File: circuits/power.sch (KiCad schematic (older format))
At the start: 37 parts, among them J5 Barrel_Jack_OD5.5_ID2.5, J6 Barrel_Jack_OD5.5_ID2.5, J7 Barrel_Jack_OD5.5_ID2.5, U4 REG_3V3, U5 MIC29302WU, U6 MIC29302WU, U7 MIC29302WU

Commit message: Sent to fab.
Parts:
- removed C1: C_1000uF, Capacitor_THT:CP_Radial_D12.5mm_P5.00mm, symbol Open_Automation:C_1000uF
- removed C2, C6: C_10uF, Capacitor_SMD:C_0603_1608Metric_Pad1.08x0.95mm_HandSolder, symbol Open_Automation:C_10uF
- removed C7, C8, C9: C_10uF_Ta, Capacitor_Tantalum_SMD:CP_EIA-6032-15_Kemet-U_Pad2.25x2.35mm_HandSolder, symbol Open_Automation:C_10uF_Ta
- removed D2: D_Zener, Diode_SMD:D_SMB_Handsoldering, symbol Open_Automation:D_Zener
- removed D4, D5, D6, D7: LED_G, LED_SMD:LED_0603_1608Metric_Pad1.05x0.95mm_HandSolder, symbol Open_Automation:LED_G
- removed J5, J6, J7: Barrel_Jack_OD5.5_ID2.5, Open_Automation:BarrelJack_OD5.5_ID2.5, symbol Open_Automation:Barrel_Jack_OD5.5_ID2.5
- removed R10, R11, R20, R7: R_1K, Resistor_SMD:R_0603_1608Metric_Pad0.98x0.95mm_HandSolder, symbol Open_Automation:R_1K
- removed R12, R13, R4: R_10K, Resistor_SMD:R_0603_1608Metric_Pad0.98x0.95mm_HandSolder, symbol Open_Automation:R_10K
- removed R14, R16, R18: R_20K, Resistor_SMD:R_0603_1608Metric_Pad0.98x0.95mm_HandSolder, symbol Open_Automation:R_20K
- removed R15: R_6.5K, Resistor_SMD:R_0603_1608Metric_Pad0.98x0.95mm_HandSolder, symbol Open_Automation:R_6.5K
- removed R17: R_2.2K, Resistor_SMD:R_0603_1608Metric_Pad0.98x0.95mm_HandSolder, symbol Open_Automation:R_2.2K
- removed R3: R_100K, Resistor_SMD:R_0603_1608Metric_Pad0.98x0.95mm_HandSolder, symbol Open_Automation:R_100K
- removed U6, U7: MIC29302WU, Package_TO_SOT_SMD:TO-263-5_TabPin3, symbol Open_Automation:MIC29302WU
- added C1: C_10uF, Capacitor_SMD:C_0603_1608Metric_Pad1.08x0.95mm_HandSolder, symbol Open_Automation:C_10uF
- added C2, C6: C_10uF_Ta, Capacitor_Tantalum_SMD:CP_EIA-6032-15_Kemet-U_Pad2.25x2.35mm_HandSolder, symbol Open_Automation:C_10uF_Ta
- added D1: D_Zener, Diode_SMD:D_SMB_Handsoldering, symbol Open_Automation:D_Zener
- added D2: LED_G, LED_SMD:LED_0603_1608Metric_Pad1.05x0.95mm_HandSolder, symbol Open_Automation:LED_G
- added J10: Barrel_Jack_OD5.5_ID2.5, Open_Automation:BarrelJack_OD5.5_ID2.5, symbol Open_Automation:Barrel_Jack_OD5.5_ID2.5
- added R31, R37: R_20K, Resistor_SMD:R_0603_1608Metric_Pad0.98x0.95mm_HandSolder, symbol Open_Automation:R_20K
- added R32: R_6.5K, Resistor_SMD:R_0603_1608Metric_Pad0.98x0.95mm_HandSolder, symbol Open_Automation:R_6.5K
- added R33, R36: R_1K, Resistor_SMD:R_0603_1608Metric_Pad0.98x0.95mm_HandSolder, symbol Open_Automation:R_1K
- added R34: R_70K, Resistor_SMD:R_0603_1608Metric_Pad0.98x0.95mm_HandSolder, symbol Open_Automation:R_70K
- added R35: R_10K, Resistor_SMD:R_0603_1608Metric_Pad0.98x0.95mm_HandSolder, symbol Open_Automation:R_10K
- added U9: MIC29302WU, Package_TO_SOT_SMD:TO-263-5_TabPin3, symbol Open_Automation:MIC29302WU
- renumbered R19 to R38, R8 to R39, U5 to U7, U4 to U8
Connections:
- net labels added: POWER, PWR_SENSE, REG_POWER
- net labels removed: BATTERY, BATT_ADC, CURRENT_SENSE, DISPLAY_EN, DISPLAY_POWER, MAIN_EN, MAIN_POWER, MAIN_POWER_IN, POWER_IN, SENSE0, SENSE1, TRIGGER0, TRIGGER1, VIOUT
- wire segments 122 -> 70
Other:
- moved on the sheet: R38, R39, U7

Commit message: finished schematic corrections, working on layout
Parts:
- removed D1: D_Zener, Diode_SMD:D_SMB_Handsoldering, symbol Open_Automation:D_Zener
- removed J10: Barrel_Jack_OD5.5_ID2.5, Open_Automation:BarrelJack_OD5.5_ID2.5, symbol Open_Automation:Barrel_Jack_OD5.5_ID2.5
- removed R32: R_6.5K, Resistor_SMD:R_0603_1608Metric_Pad0.98x0.95mm_HandSolder, symbol Open_Automation:R_6.5K
- removed U8: REG_3V3, Package_TO_SOT_SMD:TO-252-2, symbol Open_Automation:REG_3V3
- added D3: LED_G, LED_SMD:LED_0603_1608Metric_Pad1.05x0.95mm_HandSolder, symbol Open_Automation:LED_G
- added R33: R_6.8K, Resistor_SMD:R_0603_1608Metric_Pad0.98x0.95mm_HandSolder, symbol Open_Automation:R_6.8K
- added U8: REG_AMS1117-3.3, Package_TO_SOT_SMD:SOT-223-3_TabPin2, symbol Open_Automation:REG_AMS1117-3.3
- renumbered D3 to D4, R31 to R32, R33 to R34, R34 to R35, R35 to R36, R36 to R37, R37 to R38, R38 to R39, R39 to R40
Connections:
- wire segments 70 -> 66
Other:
- moved on the sheet: R37

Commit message: got board back from fab, testing
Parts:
- removed R32, R38: R_20K, Resistor_SMD:R_0603_1608Metric_Pad0.98x0.95mm_HandSolder, symbol Open_Automation:R_20K
- removed R36: R_10K, Resistor_SMD:R_0603_1608Metric_Pad0.98x0.95mm_HandSolder, symbol Open_Automation:R_10K
- removed R39: R_2.2K, Resistor_SMD:R_0603_1608Metric_Pad0.98x0.95mm_HandSolder, symbol Open_Automation:R_2.2K
- added R?: R_2.2K, Resistor_SMD:R_0402_1005Metric_Pad0.72x0.64mm_HandSolder, symbol Open_Automation:R_2.2K
- added R? (x2): R_20K, Resistor_SMD:R_0402_1005Metric_Pad0.72x0.64mm_HandSolder, symbol Open_Automation:R_20K
- added R?: R_10K_0402, Resistor_SMD:R_0402_1005Metric_Pad0.72x0.64mm_HandSolder, symbol Open_Automation:R_10K_0402
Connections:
- net 5V: now also R?.1
- net GND: now also R?.1, R?.2
- net PWR_SENSE: now also R?.2
- net REG_POWER: now also R?.1
- net at U9.5 (Feedback): now also R?.1, R?.2
- net at R33.1, U7.5 (Feedback): now also R?.2
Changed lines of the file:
@@
-$EndComp
-$Comp
-L Open_Automation:R_20K R?
-U 1 1 5FFACB63
-P 8550 4350
-AR Path="/5A7BADB8/5FFACB63" Ref="R?"  Part="1"
-AR Path="/6045445B/5FFACB63" Ref="R38"  Part="1"
-F 0 "R38" H 8600 4300 50  0000 L CNN
-F 1 "R_20K" H 8550 4200 50  0000 L CNN
-F 2 "Resistor_SMD:R_0603_1608Metric_Pad0.98x0.95mm_HandSolder" V 8480 4350 50  0001 C CNN
-F 3 "https://datasheet.lcsc.com/szlcsc/Uniroyal-Elec-0603WAF2002T5E_C4184.pdf" V 8630 4350 50  0001 C CNN
-F 4 "0603WAF2002T5E" V 8730 4450 60  0001 C CNN "Part Number"
-F 5 "C4184" H -1250 -1150 50  0001 C CNN "LCSC"
-	1    8550 4350
-	1    0    0    -1
-$EndComp
-$Comp
-L Open_Automation:R_20K R?
-U 1 1 5FFACB61
-P 4600 4150
-AR Path="/5A7BADB8/5FFACB61" Ref="R?"  Part="1"
-AR Path="/6045445B/5FFACB61" Ref="R32"  Part="1"
-F 0 "R32" V 4600 4050 50  0000 L CNN
-F 1 "R_20K" V 4700 4050 50  0000 L CNN
-F 2 "Resistor_SMD:R_0603_1608Metric_Pad0.98x0.95mm_HandSolder" V 4530 4150 50  0001 C CNN
-F 3 "https://datasheet.lcsc.com/szlcsc/Uniroyal-Elec-0603WAF2002T5E_C4184.pdf" V 4680 4150 50  0001 C CNN
-F 4 "0603WAF2002T5E" V 4780 4250 60  0001 C CNN "Part Number"
-F 5 "C4184" H -5100 2200 50  0001 C CNN "LCSC"
-	1    4600 4150
-	1    0    0    -1
 $EndComp
 $Comp
@@
 	1    0    0    -1
 $EndComp
-$Comp
-L Open_Automation:R_2.2K R?
-U 1 1 5CC27388
-P 8550 4750
-AR Path="/5A7BADB8/5CC27388" Ref="R?"  Part="1"
-AR Path="/6045445B/5CC27388" Ref="R39"  Part="1"
-F 0 "R39" H 8600 4700 50  0000 L CNN
-F 1 "R_2.2K" H 8550 4600 50  0000 L CNN
-F 2 "Resistor_SMD:R_0603_1608Metric_Pad0.98x0.95mm_HandSolder" V 8480 4750 50  0001 C CNN
-F 3 "https://datasheet.lcsc.com/szlcsc/Uniroyal-Elec-0603WAF2201T5E_C4190.pdf" V 8630 4750 50  0001 C CNN
-F 4 "0603WAF2201T5E" V 8730 4850 60  0001 C CNN "Part Number"
-F 5 "C4190" H -1250 -1150 50  0001 C CNN "LCSC"
-	1    8550 4750
-	1    0    0    -1
-$EndComp
 Wire Wire Line
 	6950 4150 6900 4150
@@
 Text HLabel 1650 1300 0    60   Input ~ 0
 REG_POWER
-$Comp
-L Open_Automation:R_10K R36
-U 1 1 60405BCA
-P 5350 1950
-F 0 "R36" H 5420 1996 50  0000 L CNN
-F 1 "R_10K" H 5420 1905 50  0000 L CNN
-F 2 "Resistor_SMD:R_0603_1608Metric_Pad0.98x0.95mm_HandSolder" V 5280 1950 50  0001 C CNN
-F 3 "https://datasheet.lcsc.com/szlcsc/Uniroyal-Elec-0603WAF1002T5E_C25804.pdf" V 5430 1950 50  0001 C CNN
-F 4 "0603WAF1002T5E" V 5530 2050 60  0001 C CNN "Part Number"
-F 5 "C25804" V 5600 1950 50  0001 C CNN "LCSC"
-	1    5350 1950
-	1    0    0    -1
-$EndComp
 $Comp
 L Open_Automation:R_70K R35
@@
 	1    0    0    -1
 $EndComp
+$Comp
+L Open_Automation:R_2.2K R?
+U 1 1 60456F03
+P 8550 4750
+F 0 "R?" V 8550 4700 50  0000 L CNN
+F 1 "R_2.2K" V 8450 4600 50  0000 L CNN
+F 2 "Resistor_SMD:R_0402_1005Metric_Pad0.72x0.64mm_HandSolder" V 8480 4750 50  0001 C CNN
+F 3 "https://datasheet.lcsc.com/szlcsc/Uniroyal-Elec-0402WGF2201TCE_C25879.pdf" V 8630 4750 50  0001 C CNN
+F 4 "C4190" V 8400 4750 50  0001 C CNN "LCSC"
+	1    8550 4750
+	1    0    0    -1
+$EndComp
+$Comp
+L Open_Automation:R_20K R?
+U 1 1 60459E2E
+P 8550 4350
+F 0 "R?" H 8620 4396 50  0000 L CNN
+F 1 "R_20K" H 8620 4305 50  0000 L CNN
+F 2 "Resistor_SMD:R_0402_1005Metric_Pad0.72x0.64mm_HandSolder" V 8480 4350 50  0001 C CNN
+F 3 "https://datasheet.lcsc.com/szlcsc/Uniroyal-Elec-0402WGF2002TCE_C25765.pdf" V 8630 4350 50  0001 C CNN
+F 4 "0402WGF2002TCE" V 8730 4450 60  0001 C CNN "Part Number"
+F 5 "C25765" V 8400 4350 50  0001 C CNN "LCSC"
+	1    8550 4350
+	1    0    0    -1
+$EndComp
+$Comp
+L Open_Automation:R_20K R?
+U 1 1 6045B596
+P 4600 4150
+F 0 "R?" V 4600 4100 50  0000 L CNN
+F 1 "R_20K" V 4700 4050 50  0000 L CNN
+F 2 "Resistor_SMD:R_0402_1005Metric_Pad0.72x0.64mm_HandSolder" V 4530 4150 50  0001 C CNN
+F 3 "https://datasheet.lcsc.com/szlcsc/Uniroyal-Elec-0402WGF2002TCE_C25765.pdf" V 4680 4150 50  0001 C CNN
+F 4 "0402WGF2002TCE" V 4780 4250 60  0001 C CNN "Part Number"
+F 5 "C25765" V 4450 4150 50  0001 C CNN "LCSC"
+	1    4600 4150
+	1    0    0    -1
+$EndComp
+$Comp
+L Open_Automation:R_10K_0402 R?
+U 1 1 60460A51
+P 5350 1950
+F 0 "R?" V 5350 1900 50  0000 L CNN
+F 1 "R_10K_0402" V 5450 1700 50  0000 L CNN
+F 2 "Resistor_SMD:R_0402_1005Metric_Pad0.72x0.64mm_HandSolder" V 5280 1950 50  0001 C CNN
+F 3 "https://datasheet.lcsc.com/szlcsc/Uniroyal-Elec-0402WGF1002TCE_C25744.pdf" V 5430 1950 50  0001 C CNN
+F 4 "0402WGF1002TCE" V 5530 2050 60  0001 C CNN "Part Number"
+F 5 "C25744" V 5600 1950 50  0001 C CNN "LCSC"
+	1    5350 1950
+	1    0    0    -1
+$EndComp

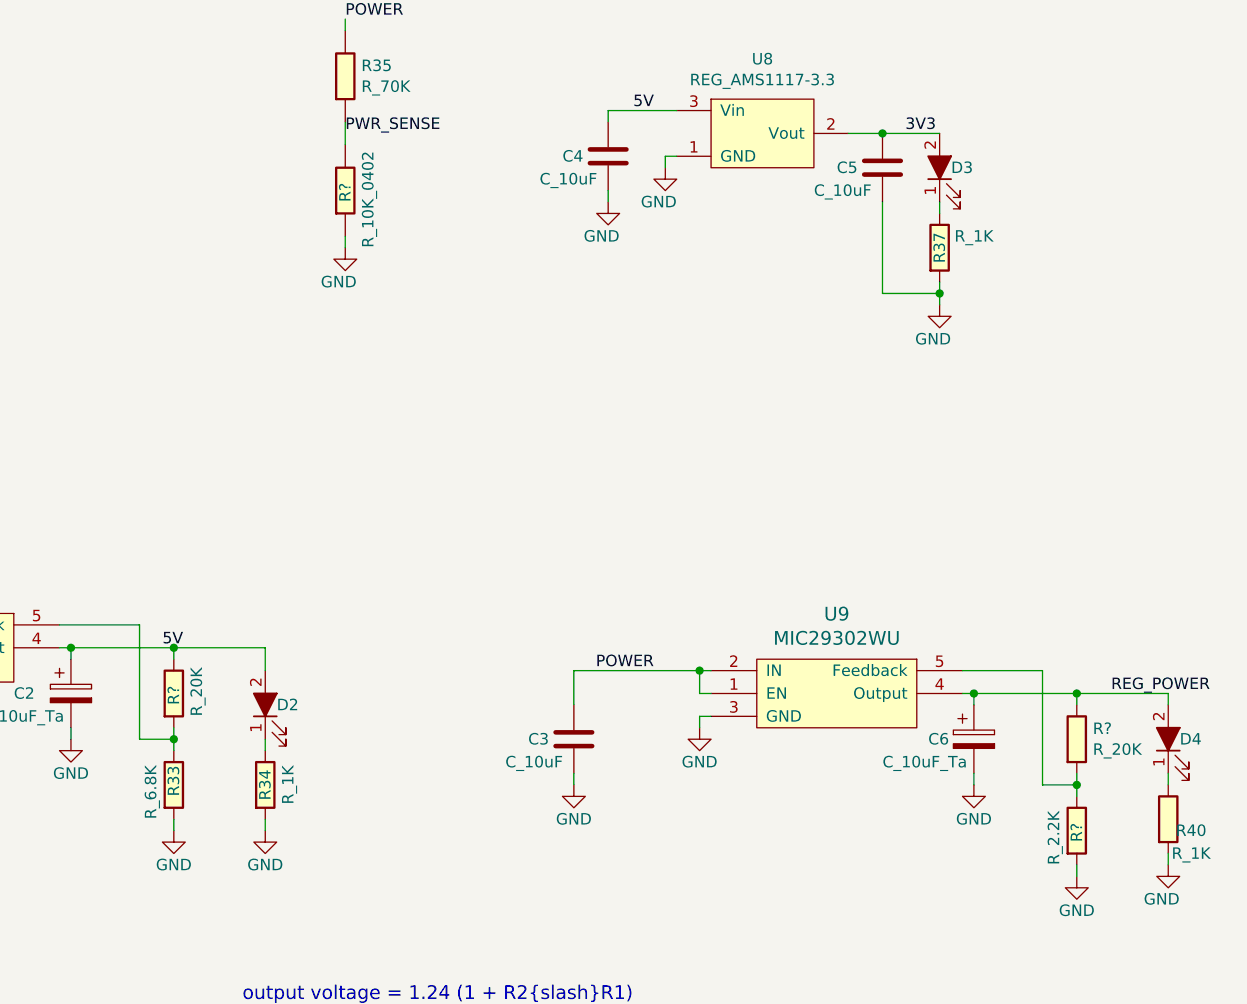
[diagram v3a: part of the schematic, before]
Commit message: modifed PoE circuit
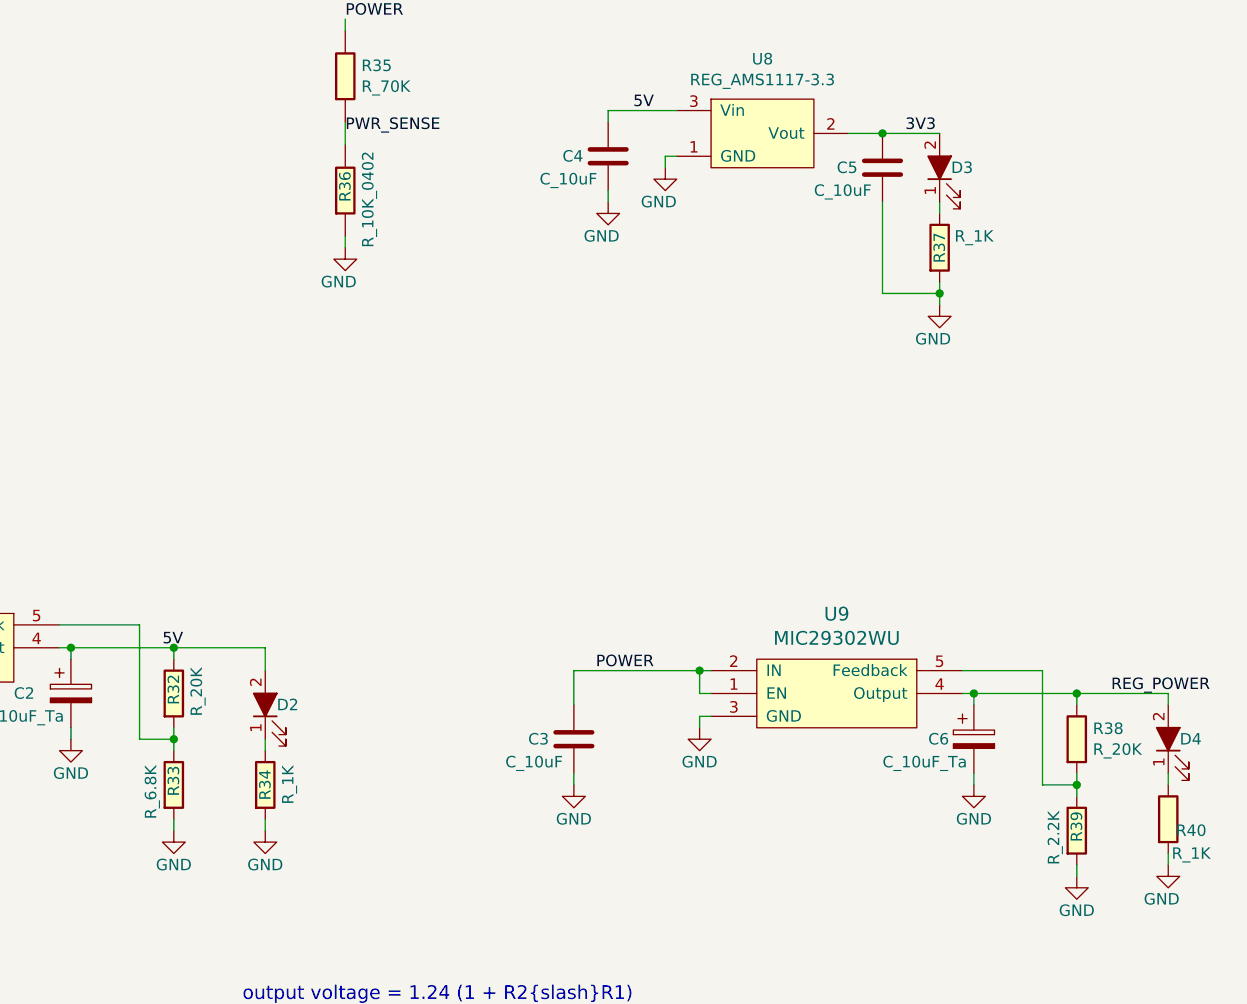
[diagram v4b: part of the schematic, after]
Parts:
- gave numbers to parts that had none: 4
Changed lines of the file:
@@
 $EndComp
 $Comp
-L Open_Automation:R_2.2K R?
+L Open_Automation:R_2.2K R39
 U 1 1 60456F03
 P 8550 4750
-F 0 "R?" V 8550 4700 50  0000 L CNN
+F 0 "R39" V 8550 4700 50  0000 L CNN
 F 1 "R_2.2K" V 8450 4600 50  0000 L CNN
 F 2 "Resistor_SMD:R_0402_1005Metric_Pad0.72x0.64mm_HandSolder" V 8480 4750 50  0001 C CNN
@@
 $EndComp
 $Comp
-L Open_Automation:R_20K R?
+L Open_Automation:R_20K R38
 U 1 1 60459E2E
 P 8550 4350
-F 0 "R?" H 8620 4396 50  0000 L CNN
+F 0 "R38" H 8620 4396 50  0000 L CNN
 F 1 "R_20K" H 8620 4305 50  0000 L CNN
 F 2 "Resistor_SMD:R_0402_1005Metric_Pad0.72x0.64mm_HandSolder" V 8480 4350 50  0001 C CNN
@@
 $EndComp
 $Comp
-L Open_Automation:R_20K R?
+L Open_Automation:R_20K R32
 U 1 1 6045B596
 P 4600 4150
-F 0 "R?" V 4600 4100 50  0000 L CNN
+F 0 "R32" V 4600 4100 50  0000 L CNN
 F 1 "R_20K" V 4700 4050 50  0000 L CNN
 F 2 "Resistor_SMD:R_0402_1005Metric_Pad0.72x0.64mm_HandSolder" V 4530 4150 50  0001 C CNN
@@
 $EndComp
 $Comp
-L Open_Automation:R_10K_0402 R?
+L Open_Automation:R_10K_0402 R36
 U 1 1 60460A51
 P 5350 1950
-F 0 "R?" V 5350 1900 50  0000 L CNN
+F 0 "R36" V 5350 1900 50  0000 L CNN
 F 1 "R_10K_0402" V 5450 1700 50  0000 L CNN
 F 2 "Resistor_SMD:R_0402_1005Metric_Pad0.72x0.64mm_HandSolder" V 5280 1950 50  0001 C CNN
